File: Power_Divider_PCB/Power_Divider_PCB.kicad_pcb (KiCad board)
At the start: 2 copper layers, 114 x 38 mm, 9 parts, among them J1 Conn_02x02_Counter_Clockwise, J2 Conn_01x02, J3 Conn_02x02_Counter_Clockwise, J4 Conn_02x02_Counter_Clockwise, J5 Conn_02x02_Counter_Clockwise, J6 Conn_02x02_Counter_Clockwise, J7 Conn_02x02_Counter_Clockwise, J8 Conn_01x02, J9 Conn_01x02

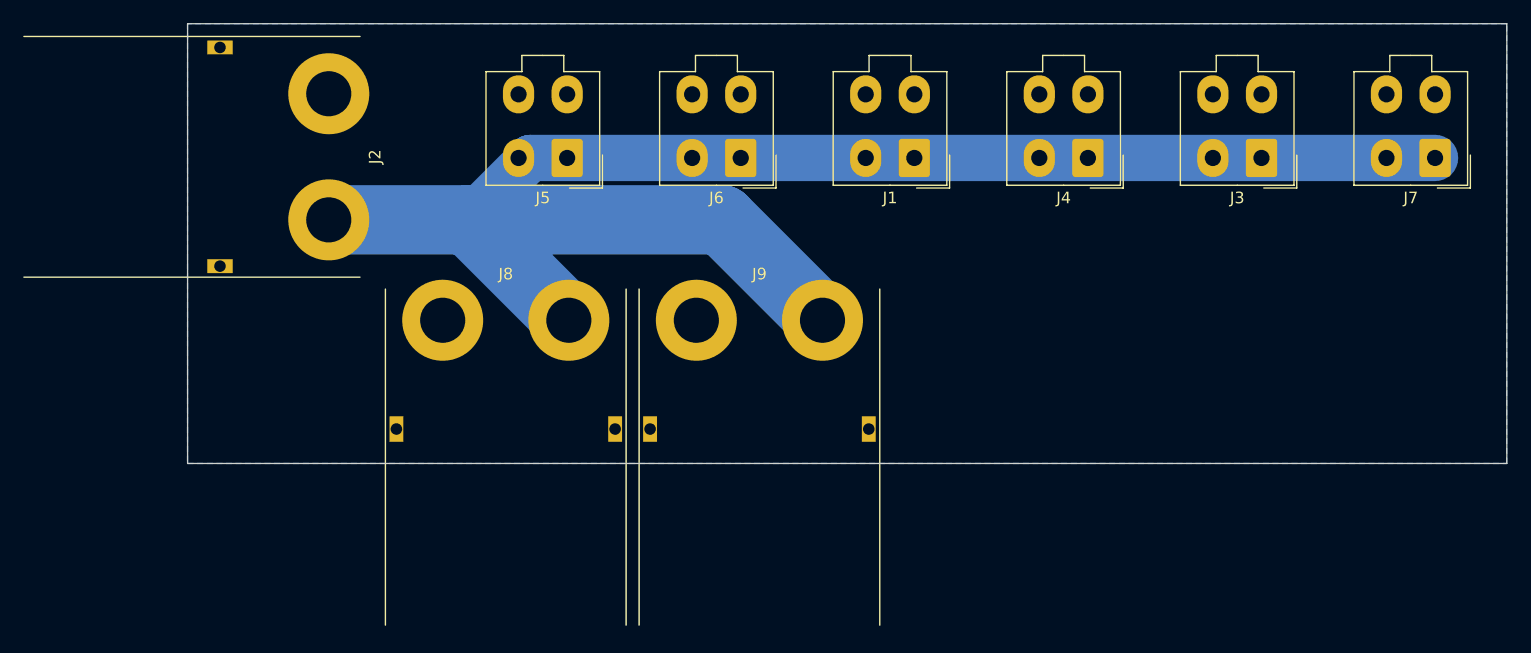
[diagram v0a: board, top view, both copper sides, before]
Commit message: Added one extra XT connector, moved existing molexes. Added Voltage polarization check: green LED - OK, red LED - wrong.
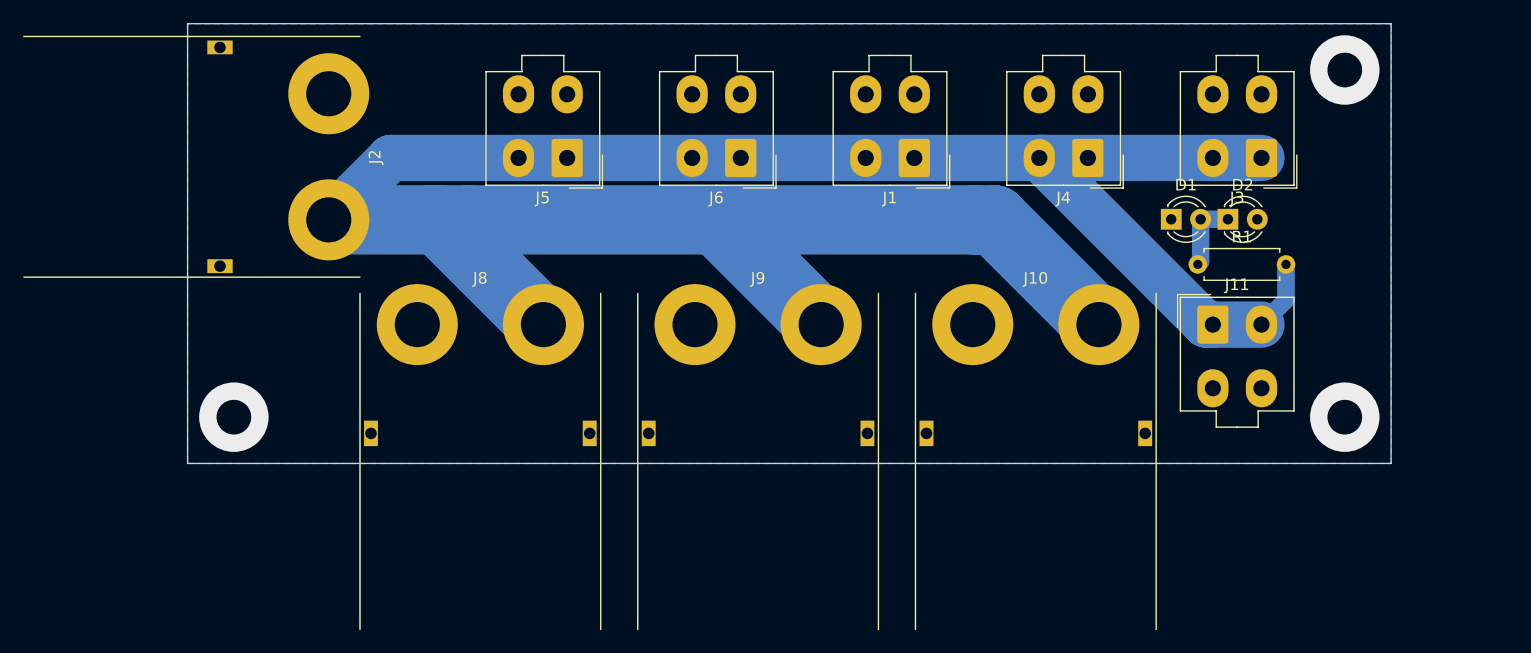
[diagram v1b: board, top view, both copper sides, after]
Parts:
- removed J7: Conn_02x02_Counter_Clockwise, Connector_Molex:Molex_Mini-Fit_Jr_5566-04A_2x02_P4.20mm_Vertical
- added D1: LED_Small, LED_THT:LED_D3.0mm, F.Cu at (118.0, 60.9)
- added D2: LED_Small, LED_THT:LED_D3.0mm, F.Cu at (122.9, 60.9)
- added J10: Conn_01x02, Connectors:XT90PW-F, F.Cu at (106.3, 70.0)
- added J11: Conn_02x02_Counter_Clockwise, Connector_Molex:Molex_Mini-Fit_Jr_5566-04A_2x02_P4.20mm_Vertical, F.Cu at (121.6, 70.0)
- added R1: R_Small, Resistor_THT:R_Axial_DIN0207_L6.3mm_D2.5mm_P7.62mm_Horizontal, F.Cu at (120.3, 64.8)
- moved J8 2.23 mm to (58.3, 70.0)
- moved J9 0.39 mm to (82.3, 70.0)
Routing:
- net HP+: track 144.3 -> 211.0 mm
- net Net-(D1-Pad2): track 0.00 -> 6.36 mm
- net (no net): vias 0 -> 3
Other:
- board size 114 x 38 mm -> 104 x 38 mm
